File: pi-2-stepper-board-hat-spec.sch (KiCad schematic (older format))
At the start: 36 parts, among them CON1 DC12v, P1 Servo, P10 BK_FEED_BYPASS, P2 Endstop1, P3 Endstop2, P4 Stepper1, P5 Stepper2, P6 COM, P7 Aux1 (SPI), P8 Aux2 (I2C)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

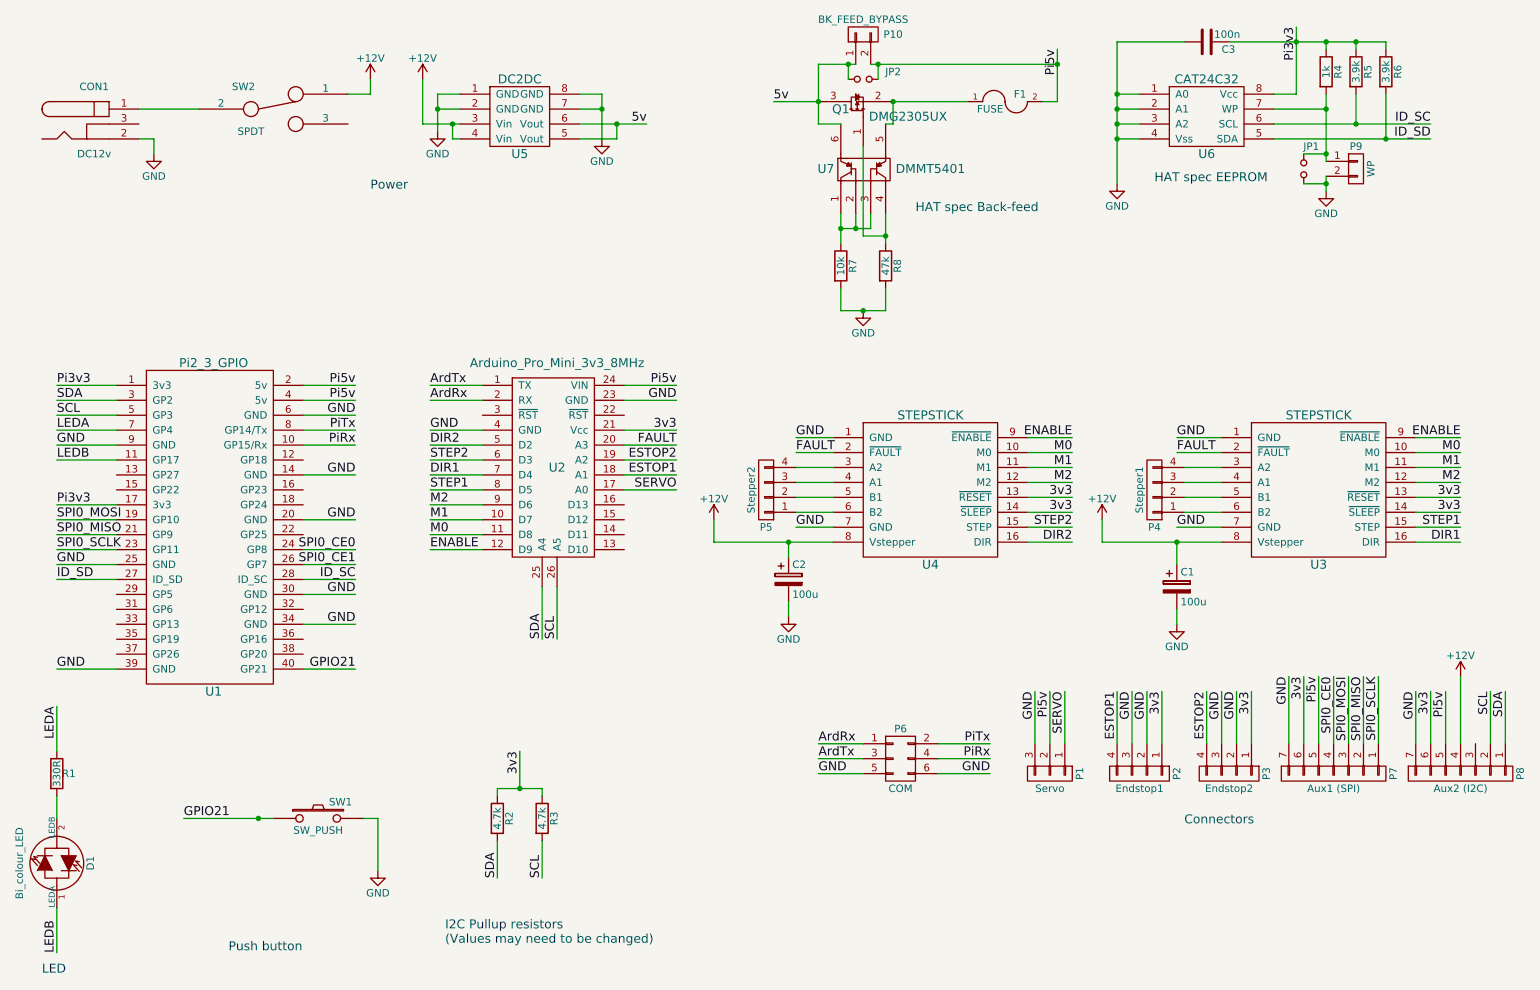
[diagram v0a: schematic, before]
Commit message: Expanded aux ports
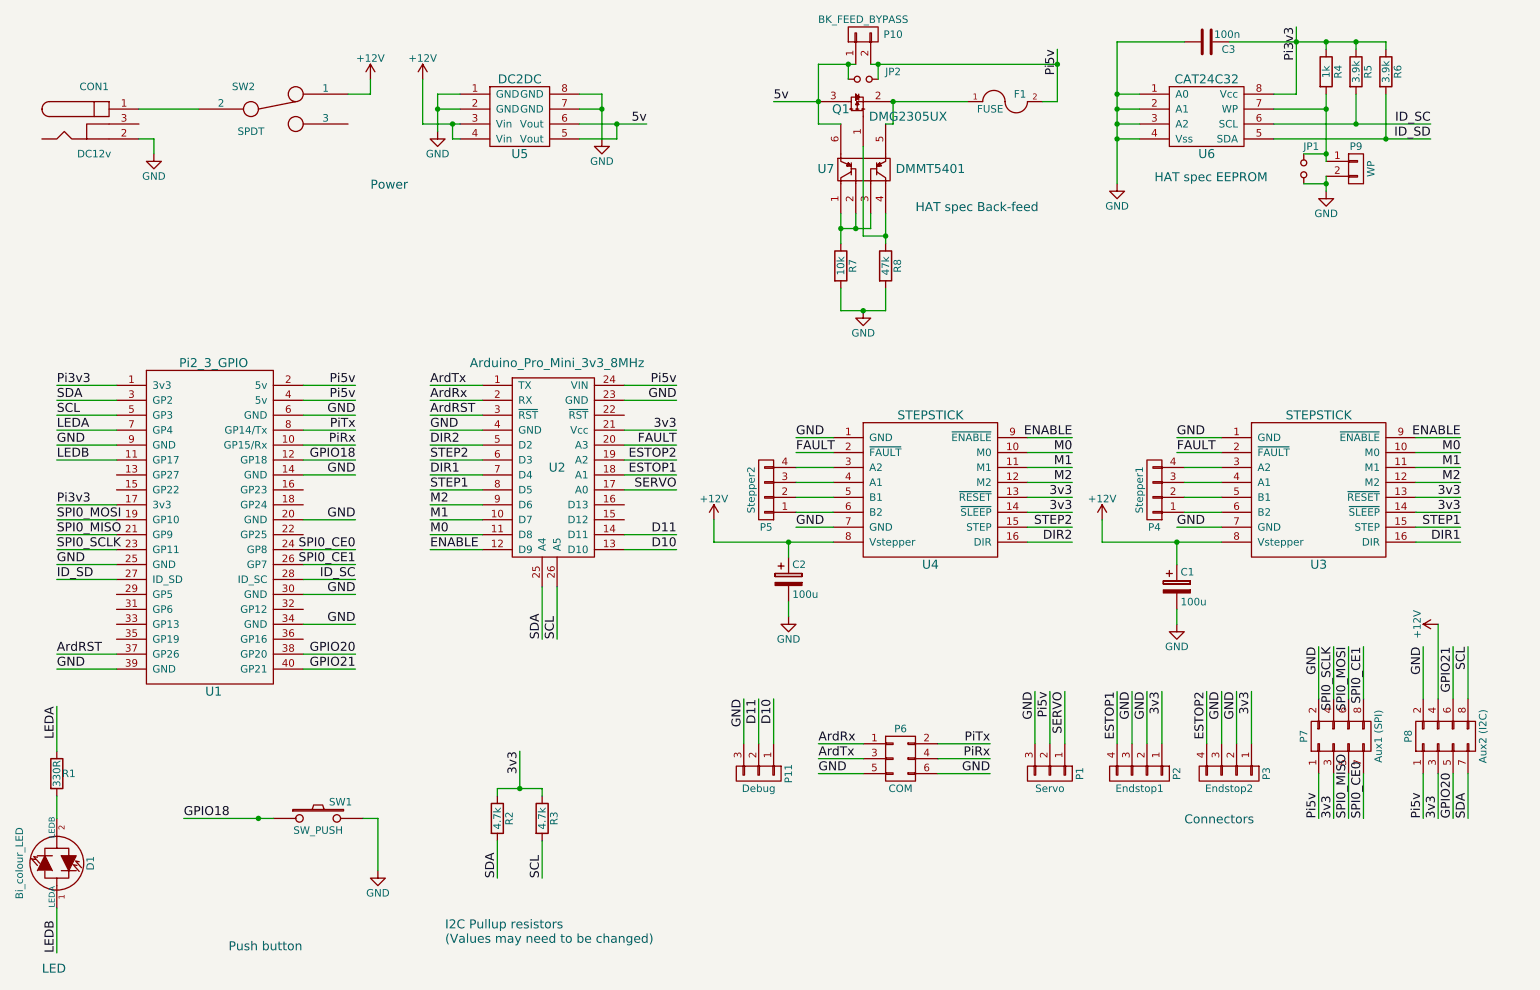
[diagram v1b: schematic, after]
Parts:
- removed P7: Aux1 (SPI), Pin_Headers:Pin_Header_Straight_1x07, symbol CONN_01X07
- removed P8: Aux2 (I2C), Pin_Headers:Pin_Header_Straight_1x07, symbol CONN_01X07
- added P11: Debug, Pin_Headers:Pin_Header_Straight_1x03, symbol CONN_01X03
- added P7: Aux1 (SPI), Pin_Headers:Pin_Header_Straight_2x04, symbol CONN_02X04
- added P8: Aux2 (I2C), Pin_Headers:Pin_Header_Straight_2x04, symbol CONN_02X04
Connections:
- net +12V: now also P8.4 (P4)
- net 3v3: now also P7.3 (P3), P8.3 (P3)
- net GND: now also P11.3 (P3), P7.2 (P2), P8.2 (P2)
- net GPIO21: now also P8.6 (P6); no longer SW1.1
- net Pi5v: now also P7.1 (P1), P8.1 (P1)
- net SCL: now also P8.8 (P8)
- net SDA: now also P8.7 (P7)
- net SPI0_CE0: now also P7.7 (P7)
- net SPI0_CE1: now also P7.8 (P8)
- net SPI0_MISO: now also P7.5 (P5)
- net SPI0_MOSI: now also P7.6 (P6)
- net SPI0_SCLK: now also P7.4 (P4)
- net GPIO18: now reaches U1.12 (GP18)
- net GPIO18: now also SW1.1
- net ArdRST: now reaches U1.37 (GP26)
- net ArdRST: now also U2.3 (~RST)
- net GPIO20: now reaches U1.38 (GP20)
- net GPIO20: now also P8.5 (P5)
- net D10: now reaches U2.13 (D10)
- net D10: now also P11.1 (P1)
- net D11: now reaches U2.14 (D11)
- net D11: now also P11.2 (P2)
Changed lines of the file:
@@
 Title "Pi 2/3 Arduino Stepper board"
 Date "2016-04-24"
-Rev "1.01b"
+Rev "Dev branch"
 Comp ""
 Comment1 "Copyright Mark Benson 2016"
@@
 Text Label 5400 3800 2    60   ~ 0
 3v3
-$Comp
-L CONN_01X07 P7
-U 1 1 56E5EFFA
-P 9800 6100
-F 0 "P7" H 9800 6500 50  0000 C CNN
-F 1 "Aux1 (SPI)" V 9900 6100 50  0000 C CNN
-F 2 "Pin_Headers:Pin_Header_Straight_1x07" H 9800 6100 50  0001 C CNN
-F 3 "" H 9800 6100 50  0000 C CNN
-	1    9800 6100
-	0    1    1    0
-$EndComp
-Text Label 9600 5450 3    60   ~ 0
+Text Label 9800 6400 1    60   ~ 0
 3v3
-Text Label 9500 5450 3    60   ~ 0
+Text Label 9700 5250 3    60   ~ 0
 GND
 $Comp
@@
 	1    0    0    -1
 $EndComp
-Text Label 2100 6400 0    60   ~ 0
-GPIO21
-Text Label 3250 5400 2    60   ~ 0
+Text Label 10600 5250 3    60   ~ 0
 GPIO21
 $Comp
@@
 	5050 3800 5400 3800
 Wire Wire Line
-	9500 5450 9500 5900
-Wire Wire Line
-	9600 5450 9600 5900
-Wire Wire Line
-	9700 5450 9700 5900
-Wire Wire Line
-	9800 5450 9800 5900
-Wire Wire Line
-	9900 5450 9900 5900
-Wire Wire Line
-	10000 5450 10000 5900
-Wire Wire Line
 	7150 6100 7500 6100
 Wire Wire Line
@@
 Wire Wire Line
 	1650 3700 1250 3700
-Wire Wire Line
-	10350 5900 10350 5550
-Wire Wire Line
-	10450 5900 10450 5550
-Wire Wire Line
-	10550 5900 10550 5550
-Wire Wire Line
-	10650 5450 10650 5900
-Text Label 10350 5550 3    60   ~ 0
-GND
-Text Label 10450 5550 3    60   ~ 0
+Text Label 10400 5250 3    60   ~ 0
+GND
+Text Label 10500 6400 1    60   ~ 0
 3v3
-Text Label 10850 5550 3    60   ~ 0
+Text Label 10700 5250 3    60   ~ 0
 SCL
 $Comp
 L +12V #PWR011
 U 1 1 56F686E7
-P 10650 5450
-F 0 "#PWR011" H 10650 5300 50  0001 C CNN
-F 1 "+12V" H 10650 5590 50  0000 C CNN
-F 2 "" H 10650 5450 50  0000 C CNN
-F 3 "" H 10650 5450 50  0000 C CNN
-	1    10650 5450
-	1    0    0    -1
-$EndComp
-$Comp
-L CONN_01X07 P8
-U 1 1 56F69224
-P 10650 6100
-F 0 "P8" H 10650 6500 50  0000 C CNN
-F 1 "Aux2 (I2C)" V 10750 6100 50  0000 C CNN
-F 2 "Pin_Headers:Pin_Header_Straight_1x07" H 10650 6100 50  0001 C CNN
-F 3 "" H 10650 6100 50  0000 C CNN
-	1    10650 6100
-	0    1    1    0
-$EndComp
-Text Label 10950 5550 3    60   ~ 0
+P 10500 5100
+F 0 "#PWR011" H 10500 4950 50  0001 C CNN
+F 1 "+12V" H 10500 5240 50  0000 C CNN
+F 2 "" H 10500 5100 50  0000 C CNN
+F 3 "" H 10500 5100 50  0000 C CNN
+	1    10500 5100
+	0    -1   -1   0
+$EndComp
+Text Label 10700 6400 1    60   ~ 0
 SDA
-Wire Wire Line
-	10950 5900 10950 5550
-Wire Wire Line
-	10850 5900 10850 5550
 $Comp
 L R R2
@@
 Text Label 3250 4700 2    60   ~ 0
 SPI0_CE1
-Text Label 9800 5450 3    60   ~ 0
+Text Label 10000 6400 1    60   ~ 0
 SPI0_CE0
-Text Label 9900 5450 3    60   ~ 0
+Text Label 9900 5250 3    60   ~ 0
 SPI0_MOSI
-Text Label 10000 5450 3    60   ~ 0
+Text Label 9900 6400 1    60   ~ 0
 SPI0_MISO
-Text Label 10100 5450 3    60   ~ 0
+Text Label 9800 5250 3    60   ~ 0
 SPI0_SCLK
-Wire Wire Line
-	10100 5900 10100 5450
 $Comp
 L C C3
@@
 Text Label 7900 5550 3    60   ~ 0
 Pi5v
-Text Label 9700 5450 3    60   ~ 0
+Text Label 9700 6400 1    60   ~ 0
 Pi5v
-Text Label 10550 5550 3    60   ~ 0
+Text Label 10400 6400 1    60   ~ 0
 Pi5v
 $Comp
@@
 Wire Wire Line
 	1250 5950 1250 5650
+$Comp
+L CONN_01X03 P11
+U 1 1 571D4AB7
+P 5950 6100
+F 0 "P11" H 5950 6300 50  0000 C CNN
+F 1 "Debug" V 6050 6100 50  0000 C CNN
+F 2 "Pin_Headers:Pin_Header_Straight_1x03" H 5950 6100 50  0001 C CNN
+F 3 "" H 5950 6100 50  0000 C CNN
+	1    5950 6100
+	0    1    1    0
+$EndComp
+Wire Wire Line
+	6050 5900 6050 5600
+Wire Wire Line
+	5950 5900 5950 5600
+Wire Wire Line
+	5850 5900 5850 5600
+Wire Wire Line
+	5050 4500 5400 4500
+Wire Wire Line
+	5050 4600 5400 4600
+Text Label 5850 5600 3    60   ~ 0
+GND
+Text Label 5950 5600 3    60   ~ 0
+D11
+Text Label 5400 4500 2    60   ~ 0
+D11
+Text Label 6050 5600 3    60   ~ 0
+D10
+Text Label 5400 4600 2    60   ~ 0
+D10
+$Comp
+L CONN_02X04 P7
+U 1 1 571D5F10
+P 9850 5850
+F 0 "P7" H 9850 6100 50  0000 C CNN
+F 1 "Aux1 (SPI)" H 9850 5600 50  0000 C CNN
+F 2 "Pin_Headers:Pin_Header_Straight_2x04" H 9850 4650 50  0001 C CNN
+F 3 "" H 9850 4650 50  0000 C CNN
+	1    9850 5850
+	0    -1   -1   0
+$EndComp
+$Comp
+L CONN_02X04 P8
+U 1 1 571D5F79
+P 10550 5850
+F 0 "P8" H 10550 6100 50  0000 C CNN
+F 1 "Aux2 (I2C)" H 10550 5600 50  0000 C CNN
+F 2 "Pin_Headers:Pin_Header_Straight_2x04" H 10550 4650 50  0001 C CNN
+F 3 "" H 10550 4650 50  0000 C CNN
+	1    10550 5850
+	0    -1   -1   0
+$EndComp
+Wire Wire Line
+	9700 6100 9700 6400
+Wire Wire Line
+	9800 6100 9800 6400
+Wire Wire Line
+	9900 6100 9900 6400
+Wire Wire Line
+	10000 6100 10000 6400
+Wire Wire Line
+	10000 5250 10000 5600
+Wire Wire Line
+	9900 5250 9900 5600
+Wire Wire Line
+	9800 5250 9800 5600
+Wire Wire Line
+	9700 5250 9700 5600
+Text Label 10000 5250 3    60   ~ 0
+SPI0_CE1
+Wire Wire Line
+	10400 6100 10400 6400
+Wire Wire Line
+	10500 6100 10500 6400
+Wire Wire Line
+	10600 6100 10600 6400
+Wire Wire Line
+	10700 6100 10700 6400
+Wire Wire Line
+	10700 5600 10700 5250
+Wire Wire Line
+	10600 5600 10600 5250
+Wire Wire Line
+	10500 5600 10500 5100
+Wire Wire Line
+	10400 5600 10400 5250
+Wire Wire Line
+	2900 4000 3250 4000
+Text Label 3250 4000 2    60   ~ 0
+GPIO18
+Text Label 2100 6400 0    60   ~ 0
+GPIO18
+Text Label 3250 5400 2    60   ~ 0
+GPIO21
+Wire Wire Line
+	2900 5300 3250 5300
+Text Label 3250 5300 2    60   ~ 0
+GPIO20
+Text Label 10600 6400 1    60   ~ 0
+GPIO20
+Wire Wire Line
+	4100 3700 3750 3700
+Wire Wire Line
+	1650 5300 1250 5300
+Text Label 3750 3700 0    60   ~ 0
+ArdRST
+Text Label 1250 5300 0    60   ~ 0
+ArdRST
 $EndSCHEMATC
